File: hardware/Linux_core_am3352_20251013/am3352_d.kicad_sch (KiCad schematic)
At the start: 1 part, among them U1 AM3352BZCZ100

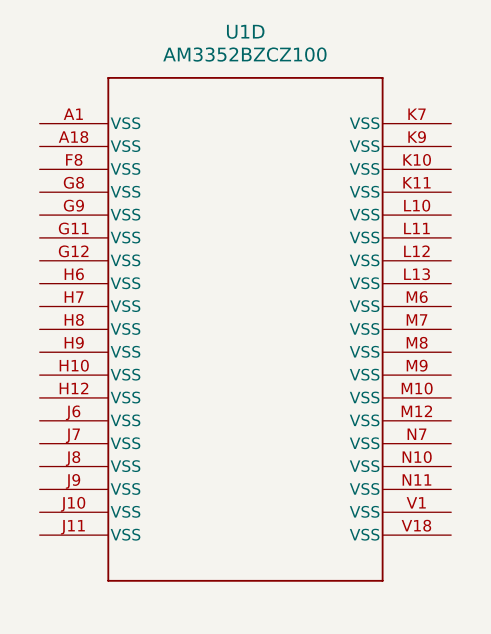
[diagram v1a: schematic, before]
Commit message: update schematic diagram
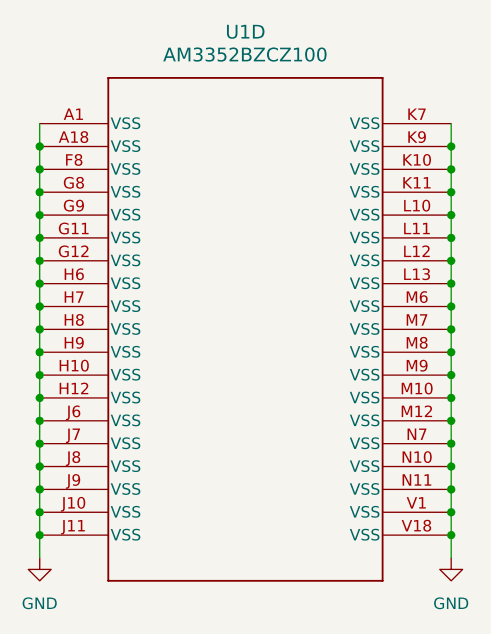
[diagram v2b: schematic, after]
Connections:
- net GND: now reaches U1.A1 (VSS)
- net GND: now also U1.A18 (VSS), U1.F8 (VSS), U1.G11 (VSS), U1.G12 (VSS), U1.G8 (VSS), U1.G9 (VSS), U1.H10 (VSS), U1.H12 (VSS), U1.H6 (VSS), U1.H7 (VSS), U1.H8 (VSS), U1.H9 (VSS), U1.J10 (VSS), U1.J11 (VSS), U1.J6 (VSS), U1.J7 (VSS), U1.J8 (VSS), U1.J9 (VSS), U1.K10 (VSS), U1.K11 (VSS), U1.K7 (VSS), U1.K9 (VSS), U1.L10 (VSS), U1.L11 (VSS), U1.L12 (VSS), U1.L13 (VSS), U1.M10 (VSS), U1.M12 (VSS), U1.M6 (VSS), U1.M7 (VSS), U1.M8 (VSS), U1.M9 (VSS), U1.N10 (VSS), U1.N11 (VSS), U1.N7 (VSS), U1.V1 (VSS), U1.V18 (VSS)
